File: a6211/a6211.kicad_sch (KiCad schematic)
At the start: 16 parts, among them J1 Conn_01x02, J2 Conn_01x02, J3 Conn_01x07, J4 Conn_01x05, J5 Conn_01x02, U1 A6211

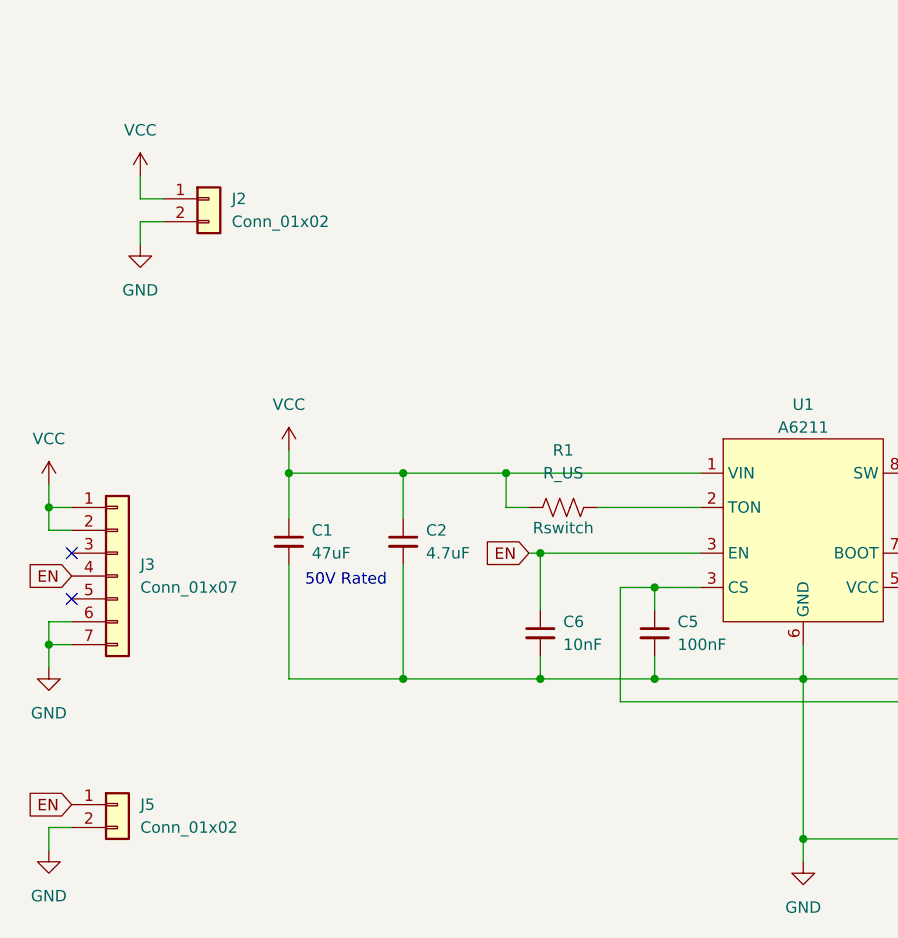
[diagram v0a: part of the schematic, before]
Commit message: A6211 - Adding comments from Tommy
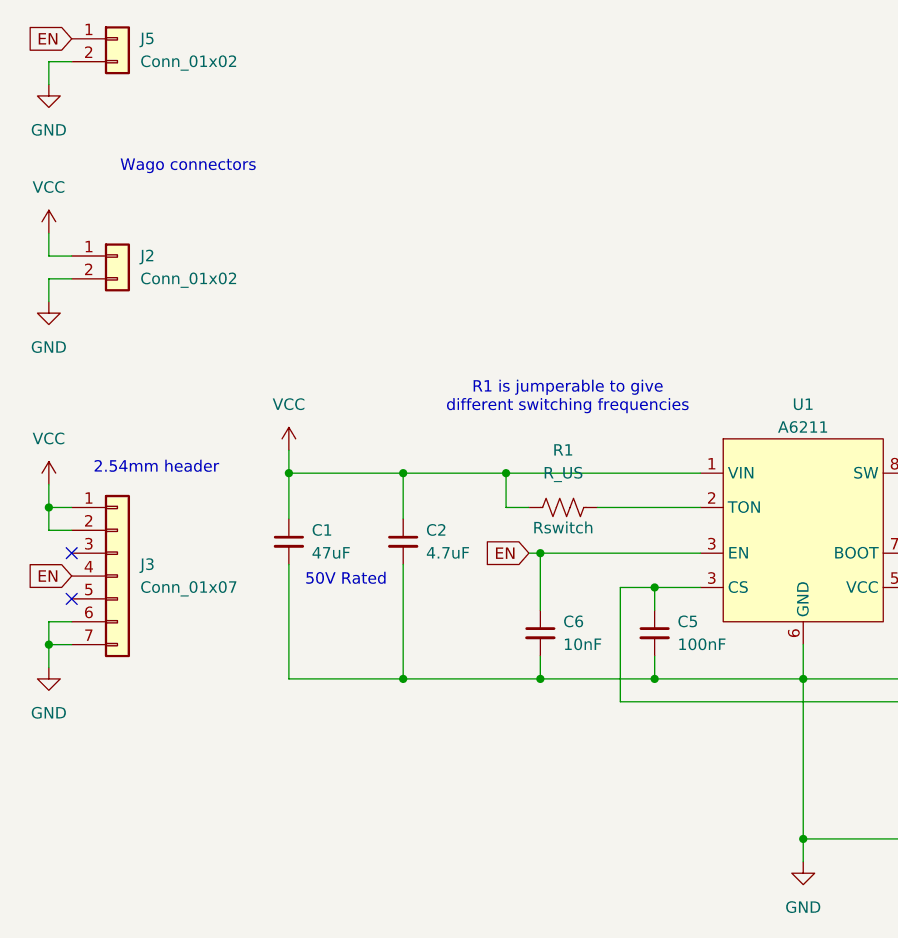
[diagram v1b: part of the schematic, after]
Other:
- note added: "2.54mm header"
- note added: "R1 is jumperable to give different switching frequencies"
- note added: "Wago connectors"
- moved on the sheet: J2, J5
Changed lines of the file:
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@@
 	(wire
 		(pts
-			(xy 48.26 62.23) (xy 48.26 59.69)
+			(xy 38.1 68.58) (xy 38.1 66.04)
 		)
 		(stroke
@@
 	(wire
 		(pts
-			(xy 38.1 127) (xy 40.64 127)
+			(xy 38.1 41.91) (xy 40.64 41.91)
 		)
 		(stroke
@@
 	(wire
 		(pts
-			(xy 48.26 59.69) (xy 50.8 59.69)
+			(xy 38.1 66.04) (xy 40.64 66.04)
 		)
 		(stroke
@@
 	(wire
 		(pts
-			(xy 48.26 54.61) (xy 48.26 57.15)
+			(xy 38.1 60.96) (xy 38.1 63.5)
 		)
 		(stroke
@@
 	(wire
 		(pts
-			(xy 48.26 57.15) (xy 50.8 57.15)
+			(xy 38.1 63.5) (xy 40.64 63.5)
 		)
 		(stroke
@@
 	(wire
 		(pts
-			(xy 38.1 129.54) (xy 38.1 127)
+			(xy 38.1 44.45) (xy 38.1 41.91)
 		)
 		(stroke
@@
 			(width 0)
 			(type default)
+		)
+	)
+	(text "2.54mm header"
+		(exclude_from_sim no)
+		(at 50.038 87.122 0)
+		(effects
+			(font
+				(size 1.27 1.27)
+				(color 255 0 45 1)
+			)
+		)
+	)
+	(text "R1 is jumperable to give \ndifferent switching frequencies"
+		(exclude_from_sim no)
+		(at 95.758 79.248 0)
+		(effects
+			(font
+				(size 1.27 1.27)
+				(color 255 0 45 1)
+			)
+		)
+	)
+	(text "Wago connectors"
+		(exclude_from_sim no)
+		(at 53.594 53.594 0)
+		(effects
+			(font
+				(size 1.27 1.27)
+				(color 255 0 45 1)
+			)
 		)
 	)
@@
 	(global_label "EN"
 		(shape input)
-		(at 40.64 124.46 180)
+		(at 40.64 39.37 180)
 		(fields_autoplaced yes)
 		(effects
@@
 		)
 		(property "Intersheetrefs" "${INTERSHEET_REFS}"
-			(at 35.1753 124.46 0)
+			(at 35.1753 39.37 0)
 			(effects
 				(font
@@
 	(symbol
 		(lib_id "Connector_Generic:Conn_01x02")
-		(at 45.72 124.46 0)
+		(at 45.72 39.37 0)
 		(unit 1)
 		(exclude_from_sim no)
@@
 		(fields_autoplaced yes)
 		(property "Reference" "J5"
-			(at 48.26 124.4599 0)
+			(at 48.26 39.3699 0)
 			(effects
 				(font
@@
 		)
 		(property "Value" "Conn_01x02"
-			(at 48.26 126.9999 0)
+			(at 48.26 41.9099 0)
 			(effects
 				(font
@@
 		)
 		(property "Footprint" "Connector_PinHeader_2.54mm:PinHeader_1x02_P2.54mm_Vertical"
-			(at 45.72 124.46 0)
+			(at 45.72 39.37 0)
 			(effects
 				(font
@@
 		)
 		(property "Datasheet" "~"
-			(at 45.72 124.46 0)
+			(at 45.72 39.37 0)
 			(effects
 				(font
@@
 		)
 		(property "Description" "Generic connector, single row, 01x02, script generated (kicad-library-utils/schlib/autogen/connector/)"
-			(at 45.72 124.46 0)
+			(at 45.72 39.37 0)
 			(effects
 				(font
@@
 	(symbol
 		(lib_id "Connector_Generic:Conn_01x02")
-		(at 55.88 57.15 0)
+		(at 45.72 63.5 0)
 		(unit 1)
 		(exclude_from_sim no)
@@
 		(fields_autoplaced yes)
 		(property "Reference" "J2"
-			(at 58.42 57.1499 0)
+			(at 48.26 63.4999 0)
 			(effects
 				(font
@@
 		)
 		(property "Value" "Conn_01x02"
-			(at 58.42 59.6899 0)
+			(at 48.26 66.0399 0)
 			(effects
 				(font
@@
 		)
 		(property "Footprint" ""
-			(at 55.88 57.15 0)
+			(at 45.72 63.5 0)
 			(effects
 				(font
@@
 		)
 		(property "Datasheet" "~"
-			(at 55.88 57.15 0)
+			(at 45.72 63.5 0)
 			(effects
 				(font
@@
 		)
 		(property "Description" "Generic connector, single row, 01x02, script generated (kicad-library-utils/schlib/autogen/connector/)"
-			(at 55.88 57.15 0)
+			(at 45.72 63.5 0)
 			(effects
 				(font
@@
 	(symbol
 		(lib_id "power:GND")
-		(at 48.26 62.23 0)
+		(at 38.1 68.58 0)
 		(unit 1)
 		(exclude_from_sim no)
@@
 		(fields_autoplaced yes)
 		(property "Reference" "#PWR06"
-			(at 48.26 68.58 0)
+			(at 38.1 74.93 0)
 			(effects
 				(font
@@
 		)
 		(property "Value" "GND"
-			(at 48.26 67.31 0)
+			(at 38.1 73.66 0)
 			(effects
 				(font
@@
 		)
 		(property "Footprint" ""
-			(at 48.26 62.23 0)
+			(at 38.1 68.58 0)
 			(effects
 				(font
@@
 		)
 		(property "Datasheet" ""
-			(at 48.26 62.23 0)
+			(at 38.1 68.58 0)
 			(effects
 				(font
@@
 		)
 		(property "Description" "Power symbol creates a global label with name \"GND\" , ground"
-			(at 48.26 62.23 0)
+			(at 38.1 68.58 0)
 			(effects
 				(font
@@
 	(symbol
 		(lib_id "power:VCC")
-		(at 48.26 54.61 0)
+		(at 38.1 60.96 0)
 		(unit 1)
 		(exclude_from_sim no)
@@
 		(fields_autoplaced yes)
 		(property "Reference" "#PWR05"
-			(at 48.26 58.42 0)
+			(at 38.1 64.77 0)
 			(effects
 				(font
@@
 		)
 		(property "Value" "VCC"
-			(at 48.26 49.53 0)
+			(at 38.1 55.88 0)
 			(effects
 				(font
@@
 		)
 		(property "Footprint" ""
-			(at 48.26 54.61 0)
+			(at 38.1 60.96 0)
 			(effects
 				(font
@@
 		)
 		(property "Datasheet" ""
-			(at 48.26 54.61 0)
+			(at 38.1 60.96 0)
 			(effects
 				(font
@@
 		)
 		(property "Description" "Power symbol creates a global label with name \"VCC\""
-			(at 48.26 54.61 0)
+			(at 38.1 60.96 0)
 			(effects
 				(font
@@
 	(symbol
 		(lib_id "power:GND")
-		(at 38.1 129.54 0)
+		(at 38.1 44.45 0)
 		(unit 1)
 		(exclude_from_sim no)
@@
 		(fields_autoplaced yes)
 		(property "Reference" "#PWR07"
-			(at 38.1 135.89 0)
+			(at 38.1 50.8 0)
 			(effects
 				(font
@@
 		)
 		(property "Value" "GND"
-			(at 38.1 134.62 0)
+			(at 38.1 49.53 0)
 			(effects
 				(font
@@
 		)
 		(property "Footprint" ""
-			(at 38.1 129.54 0)
+			(at 38.1 44.45 0)
 			(effects
 				(font
@@
 		)
 		(property "Datasheet" ""
-			(at 38.1 129.54 0)
+			(at 38.1 44.45 0)
 			(effects
 				(font
@@
 		)
 		(property "Description" "Power symbol creates a global label with name \"GND\" , ground"
-			(at 38.1 129.54 0)
-			(effects
-				(font
+			(at 38.1 44.45 0)
+			(effects
+				(font

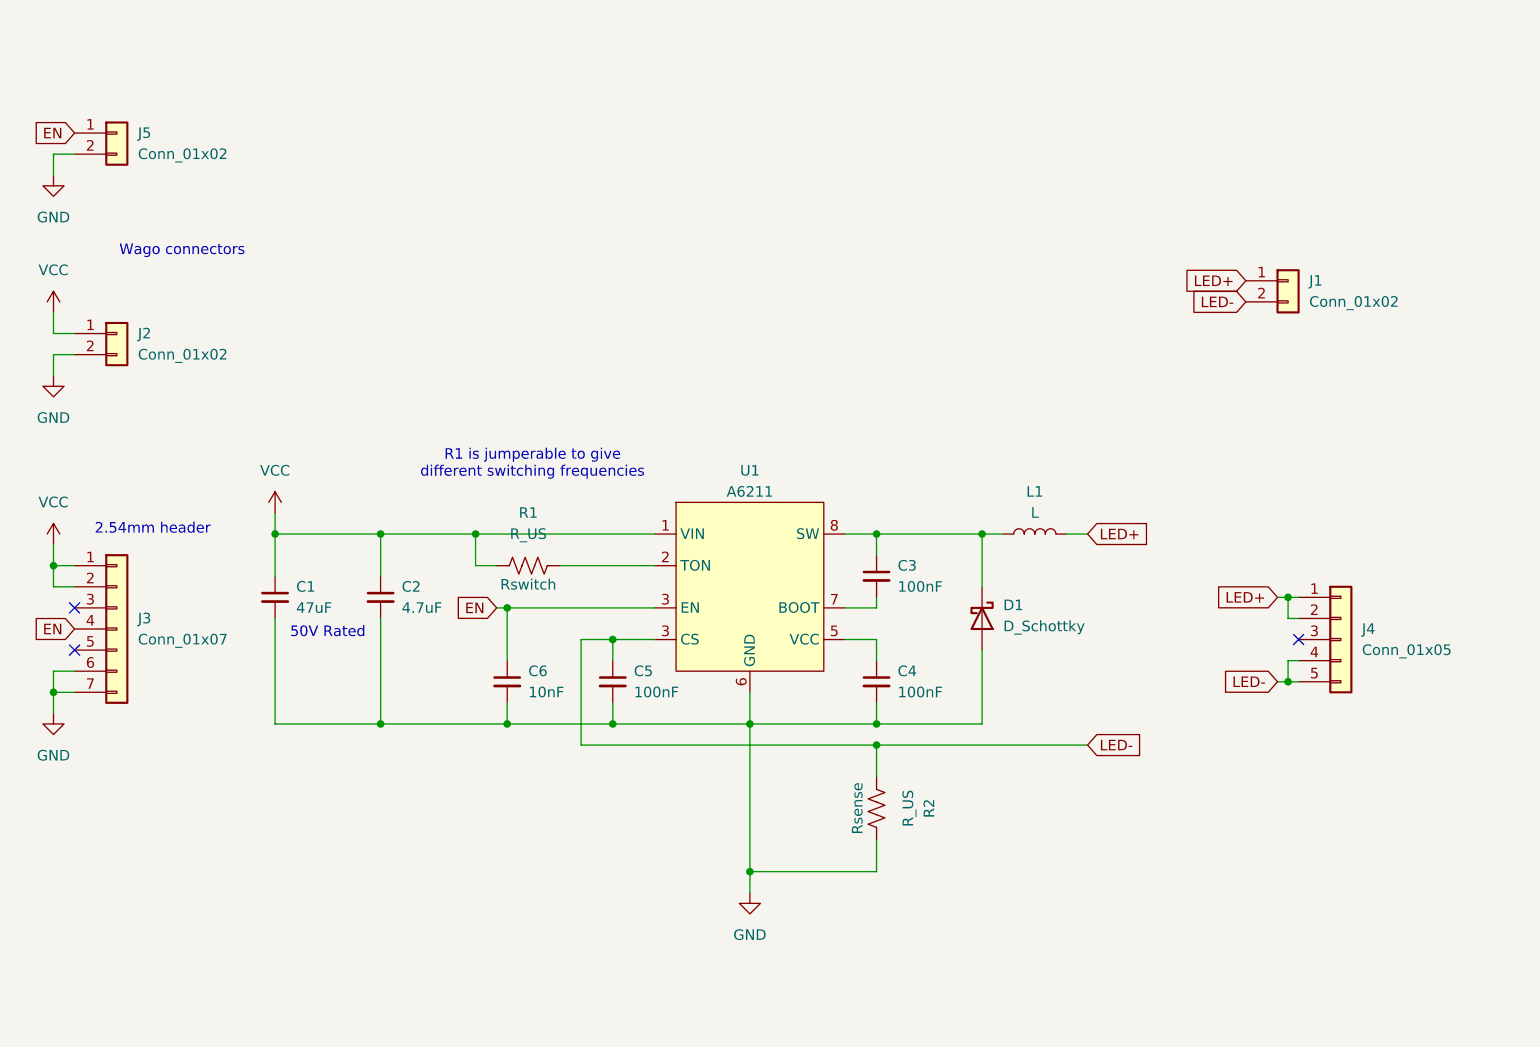
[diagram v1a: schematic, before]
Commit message: A6211 Routing and Layout Completed
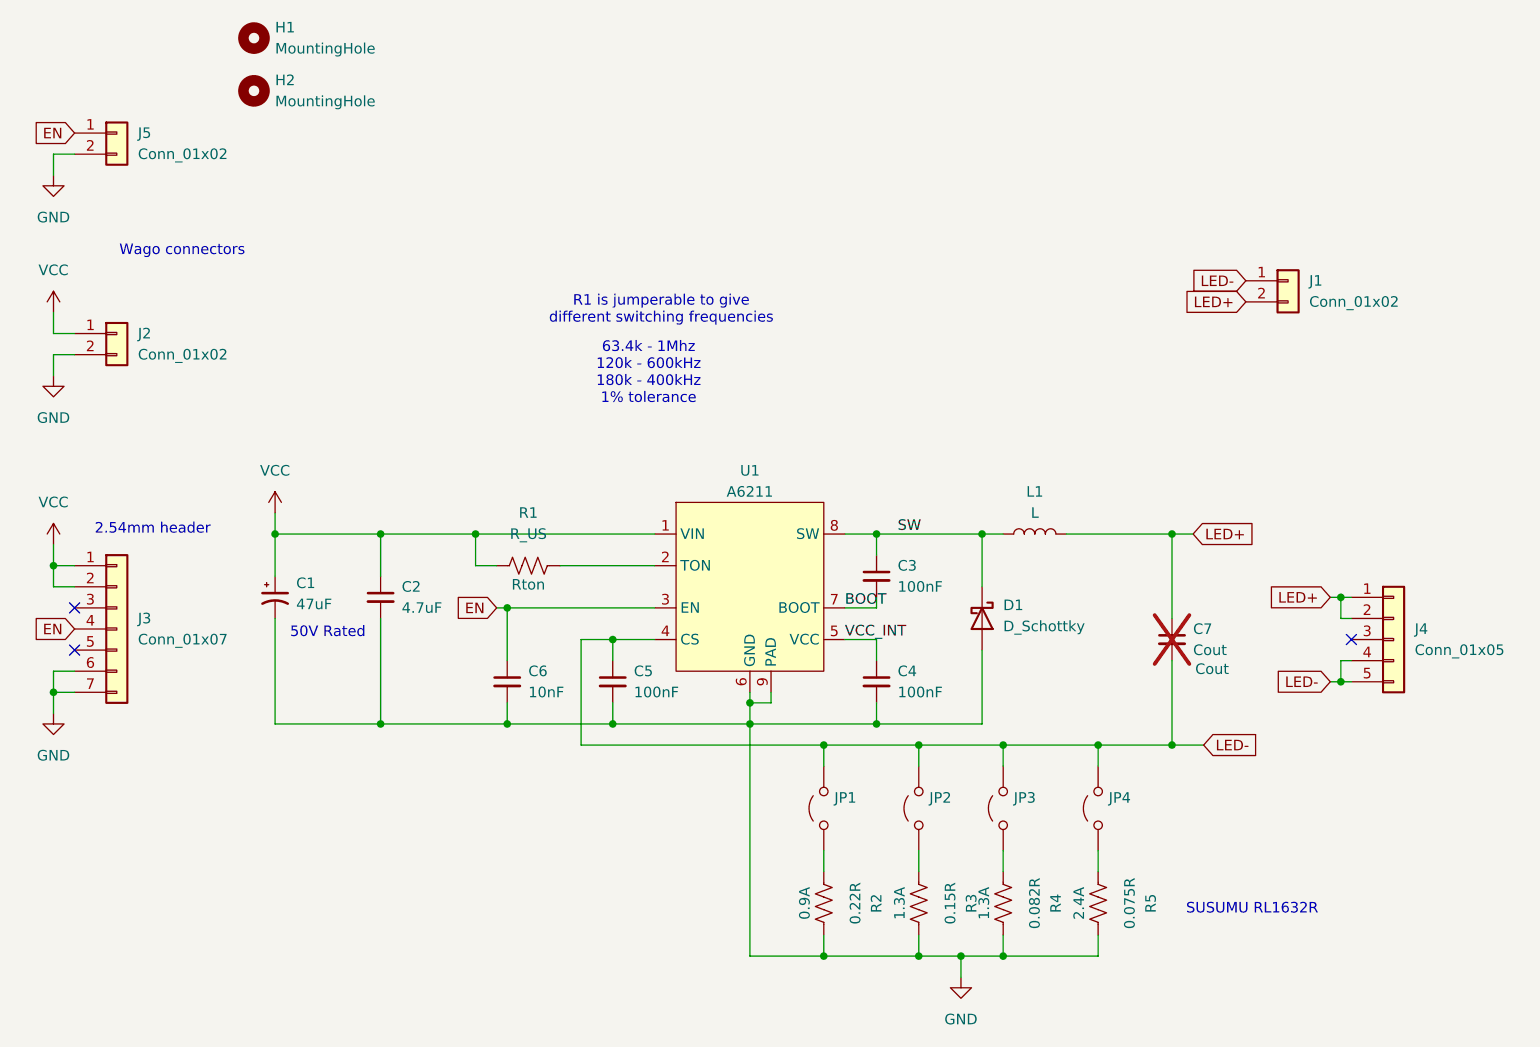
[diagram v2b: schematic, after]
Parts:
- removed C1: 47uF, Capacitor_THT:CP_Radial_D5.0mm_P2.00mm, symbol Device:C_Small
- added C1: 47uF, Capacitor_SMD:CP_Elec_8x10, symbol Device:C_Polarized_Small_US
- added C7: Cout, Capacitor_SMD:C_0603_1608Metric_Pad1.08x0.95mm_HandSolder, symbol Device:C_Small
- added H1, H2: MountingHole, MountingHole:MountingHole_3.2mm_M3, symbol Mechanical:MountingHole
- added JP1, JP2, JP3, JP4: ~, Jumper:SolderJumper-2_P1.3mm_Open_RoundedPad1.0x1.5mm, symbol Jumper:Jumper_2_Open
- added R3: 0.15R, Resistor_SMD:R_0612_1632Metric_Pad1.18x3.40mm_HandSolder, symbol Device:R_US
- added R4: 0.082R, Resistor_SMD:R_0612_1632Metric_Pad1.18x3.40mm_HandSolder, symbol Device:R_US
- added R5: 0.075R, Resistor_SMD:R_0612_1632Metric_Pad1.18x3.40mm_HandSolder, symbol Device:R_US
- C2: footprint (none) -> Capacitor_SMD:C_1206_3216Metric
- D1: footprint (none) -> Diode_SMD:D_SMC; MFR (none) -> B560C-13-F
- J1, J2: footprint (none) -> MHCI:2060-452-998-404 Wago; MFR (none) -> 2060-452/998-404
- L1: footprint (none) -> Inductor_SMD:L_10.4x10.4_H4.8; MFR (none) -> B82464G4103M
- R1: footprint (none) -> Resistor_SMD:R_0603_1608Metric_Pad0.98x0.95mm_HandSolder
- R2: value R_US -> 0.22R; footprint (none) -> Resistor_SMD:R_0612_1632Metric_Pad1.18x3.40mm_HandSolder; MFR (none) -> RL1632R-R220-F
- U1: MFR (none) -> A6211GLJTR-T
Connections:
- net GND: now also U1.9 (PAD), C1.2, R3.2, R4.2, R5.2
- net LED+: now also J1.2 (Pin_2), C7.1; no longer J1.1 (Pin_1)
- net LED-: now also J1.1 (Pin_1), U1.4 (CS), C7.2, JP1.2 (B), JP2.2 (B), JP3.2 (B), JP4.2 (B); no longer J1.2 (Pin_2), R2.1, U1.3 (EN)
- net VCC: now also C1.1
- net VCC_INT: now reaches C4.1, U1.5 (VCC)
- net BOOT: now reaches C3.2, U1.7 (BOOT)
- net SW: now reaches C3.1, D1.1 (K), L1.1, U1.8 (SW)
- new net: JP1.1 (A), R2.1
- new net: JP3.1 (A), R4.1
- new net: JP2.1 (A), R3.1
- new net: JP4.1 (A), R5.1
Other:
- note added: "63.4k - 1Mhz 120k - 600kHz 180k - 400kHz 1% tolerance"
- note added: "SUSUMU RL1632R"
- moved on the sheet: J4, R2

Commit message: A6211 Production v1
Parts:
- added HS1: Heatsink, MHCI:HSB02-101007, symbol Mechanical:Heatsink
- R2, R3, R4, R5: footprint Resistor_SMD:R_0612_1632Metric_Pad1.18x3.40mm_HandSolder -> Resistor_SMD:R_1206_3216Metric
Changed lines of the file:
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@@
 	(text "63.4k - 1Mhz\n120k - 600kHz\n180k - 400kHz\n1% tolerance"
 		(exclude_from_sim no)
-		(at 109.728 68.326 0)
+		(at 96.774 78.994 0)
 		(effects
 			(font
@@
 	(text "R1 is jumperable to give \ndifferent switching frequencies"
 		(exclude_from_sim no)
-		(at 111.252 60.706 0)
+		(at 97.282 70.104 0)
 		(effects
 			(font
@@
 			)
 		)
-		(property "Footprint" "Resistor_SMD:R_0612_1632Metric_Pad1.18x3.40mm_HandSolder"
+		(property "Footprint" "Resistor_SMD:R_1206_3216Metric"
 			(at 153.416 132.334 90)
 			(effects
@@
 			)
 		)
-		(property "Description" "1.3A"
+		(property "Description" "2.4A"
 			(at 150.114 132.08 90)
 			(effects
@@
 			)
 		)
-		(property "Footprint" "Resistor_SMD:R_0612_1632Metric_Pad1.18x3.40mm_HandSolder"
+		(property "Footprint" "Resistor_SMD:R_1206_3216Metric"
 			(at 131.826 132.334 90)
 			(effects
@@
 	)
 	(symbol
+		(lib_id "Mechanical:Heatsink")
+		(at 118.11 53.34 0)
+		(unit 1)
+		(exclude_from_sim yes)
+		(in_bom yes)
+		(on_board yes)
+		(dnp no)
+		(fields_autoplaced yes)
+		(property "Reference" "HS1"
+			(at 121.92 50.1649 0)
+			(effects
+				(font
+					(size 1.27 1.27)
+				)
+				(justify left)
+			)
+		)
+		(property "Value" "Heatsink"
+			(at 121.92 52.7049 0)
+			(effects
+				(font
+					(size 1.27 1.27)
+				)
+				(justify left)
+			)
+		)
+		(property "Footprint" "MHCI:HSB02-101007"
+			(at 118.4148 53.34 0)
+			(effects
+				(font
+					(size 1.27 1.27)
+				)
+				(hide yes)
+			)
+		)
+		(property "Datasheet" "~"
+			(at 118.4148 53.34 0)
+			(effects
+				(font
+					(size 1.27 1.27)
+				)
+				(hide yes)
+			)
+		)
+		(property "Description" "Heatsink"
+			(at 118.11 53.34 0)
+			(effects
+				(font
+					(size 1.27 1.27)
+				)
+				(hide yes)
+			)
+		)
+		(instances
+			(project ""
+				(path "/0eae7fad-4295-4de1-8a09-6528fc5757a4"
+					(reference "HS1")
+					(unit 1)
+				)
+			)
+		)
+	)
+	(symbol
 		(lib_id "Device:C_Small")
 		(at 92.71 105.41 0)
@@
 			)
 		)
-		(property "Footprint" "Resistor_SMD:R_0612_1632Metric_Pad1.18x3.40mm_HandSolder"
+		(property "Footprint" "Resistor_SMD:R_1206_3216Metric"
 			(at 143.256 132.334 90)
 			(effects
@@
 			)
 		)
-		(property "Footprint" "Resistor_SMD:R_0612_1632Metric_Pad1.18x3.40mm_HandSolder"
+		(property "Footprint" "Resistor_SMD:R_1206_3216Metric"
 			(at 164.846 132.334 90)
 			(effects
@@
 			)
 		)
-		(property "Description" "2.4A"
+		(property "Description" "2.7A"
 			(at 161.544 132.08 90)
 			(effects

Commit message: A6211 BOM files
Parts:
- D1: value D_Schottky -> Diode
- L1: value L -> Inductor
- R1: value R_US -> 120k
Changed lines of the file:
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@@
 			)
 		)
-		(property "Value" "L"
+		(property "Value" "Inductor"
 			(at 156.21 85.09 90)
 			(effects
@@
 			)
 		)
-		(property "Value" "R_US"
+		(property "Value" "120k"
 			(at 95.25 87.63 90)
 			(effects
@@
 			)
 		)
-		(property "Value" "D_Schottky"
+		(property "Value" "Diode"
 			(at 152.4 98.7424 90)
 			(effects
